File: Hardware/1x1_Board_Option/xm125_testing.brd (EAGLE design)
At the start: 25.4 x 25.4 mm, 29 parts, among them J1 QWIIC_RIGHT_ANGLE, J2 QWIIC_RIGHT_ANGLE

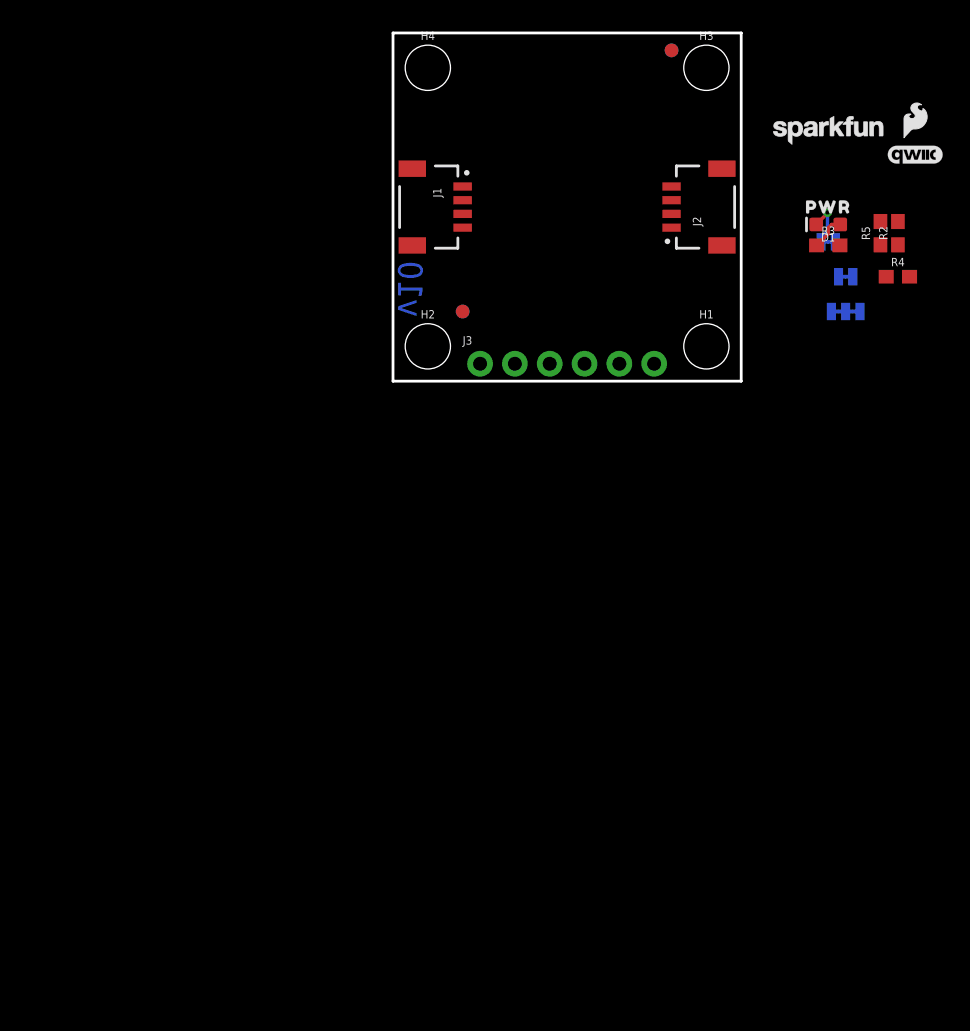
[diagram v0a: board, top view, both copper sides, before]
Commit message: Addition of initial Hardware files for breakout
We will be doing a breakout with this board, no need for 1x1 and thing+ breakout files. Will be keeping until official product definition is given
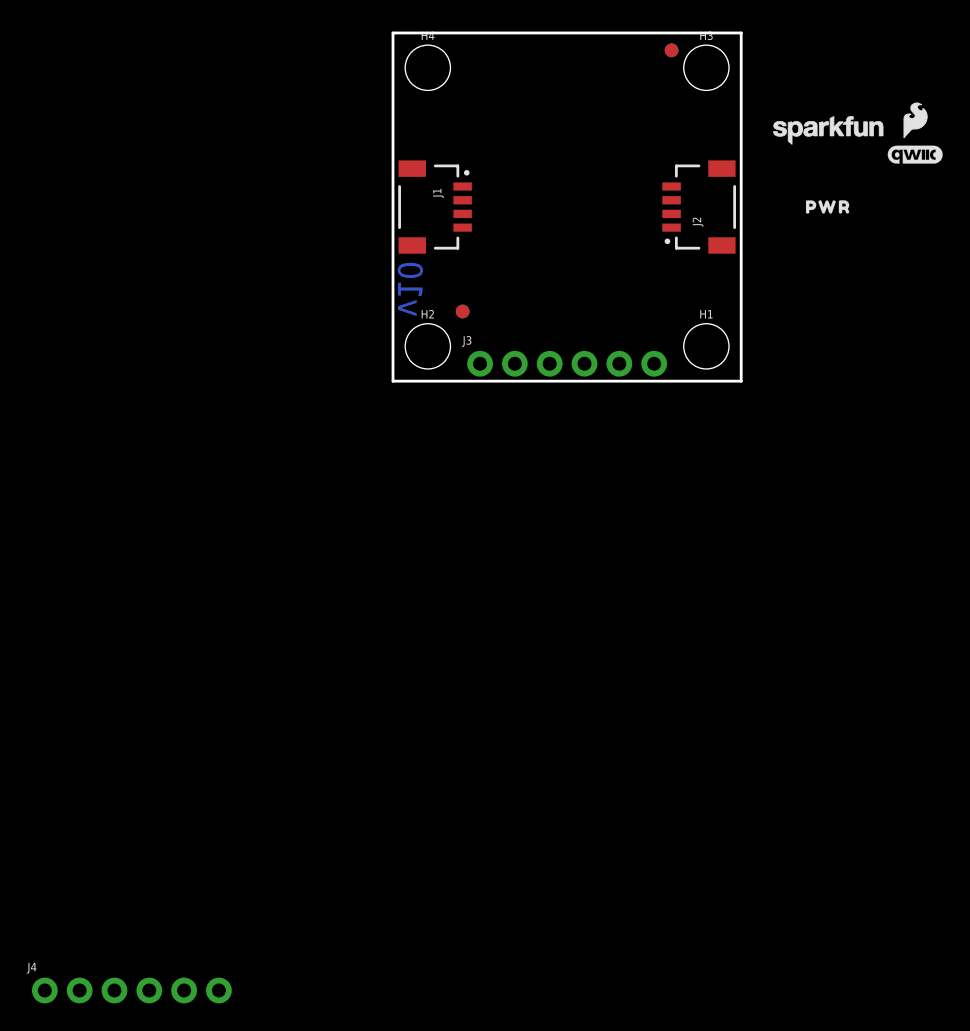
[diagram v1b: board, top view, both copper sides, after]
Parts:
- removed D1: Red, SparkFun-LED:LED-0603
- removed I2C: JUMPER-SMT_3_2-NC_TRACE_SILK, SparkFun-Jumpers:SMT-JUMPER_3_2-NC_TRACE_SILK
- removed JP2, LED: JUMPER-SMT_2_NC_TRACE_SILK, SparkFun-Jumpers:SMT-JUMPER_2_NC_TRACE_SILK
- removed R2, R5: 2.2k, SparkFun-Resistors:0603
- removed R3: 4.7k, SparkFun-Resistors:0603
- removed R4: 10k, SparkFun-Resistors:0603
- added J4: (no value), SparkFun-Connectors:1X06_NO_SILK
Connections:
- removed net !INT: J3.6, R4.1
- removed net 3.3V: J1.2, J2.2, J3.2
- removed net 3.3V_SW: I2C.2, JP2.2, R3.2
- removed net DISABLE: J3.5
- removed net GND: J1.1, J2.1, J3.1, LED.1
- removed net N$1: D1.C, LED.2
- removed net N$2: I2C.3, R2.2
- removed net N$4: D1.A, R3.1
- removed net N$5: JP2.1, R4.2
- removed net N$6: I2C.1, R5.2
- removed net SCL: J1.4, J2.4, J3.4, R5.1
- removed net SDA: J1.3, J2.3, J3.3, R2.1
- new net 1: J1.1, J2.1
- new net 2: J1.2, J2.2
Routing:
- net N$1: track 3.55 -> 0.00 mm, vias 1 -> 0
- net N$4: track 2.61 -> 0.00 mm
